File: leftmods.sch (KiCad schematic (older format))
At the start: 13 parts

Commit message: Fix left shift, associate MX footprints
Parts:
- K_LA1, K_LA2, K_LA3, K_LC2, K_LW1, K_LW2: footprint (none) -> MX_Alps_Hybrid:MX-1.5U
- K_LC1: footprint (none) -> MX_Alps_Hybrid:MX-1.25U
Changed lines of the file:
@@
 F 0 "K_LC1" H 4250 4825 60  0000 C CNN
 F 1 "MX-1.25U" H 4250 4750 20  0000 C CNN
-F 2 "" H 4225 4675 60  0001 C CNN
+F 2 "MX_Alps_Hybrid:MX-1.25U" H 4225 4675 60  0001 C CNN
 F 3 "" H 4225 4675 60  0001 C CNN
 	1    4250 4700
@@
 F 0 "K_LC2" H 4250 5400 60  0000 C CNN
 F 1 "MX-1.5U" H 4250 5325 20  0000 C CNN
-F 2 "" H 4225 5250 60  0001 C CNN
+F 2 "MX_Alps_Hybrid:MX-1.5U" H 4225 5250 60  0001 C CNN
 F 3 "" H 4225 5250 60  0001 C CNN
 	1    4250 5275
@@
 F 0 "K_LW2" H 4800 4825 60  0000 C CNN
 F 1 "MX-1.5U" H 4800 4750 20  0000 C CNN
-F 2 "" H 4775 4675 60  0001 C CNN
+F 2 "MX_Alps_Hybrid:MX-1.5U" H 4775 4675 60  0001 C CNN
 F 3 "" H 4775 4675 60  0001 C CNN
 	1    4800 4700
@@
 F 0 "K_LA1" H 4800 5400 60  0000 C CNN
 F 1 "MX-1.5U" H 4800 5325 20  0000 C CNN
-F 2 "" H 4775 5250 60  0001 C CNN
+F 2 "MX_Alps_Hybrid:MX-1.5U" H 4775 5250 60  0001 C CNN
 F 3 "" H 4775 5250 60  0001 C CNN
 	1    4800 5275
@@
 F 0 "K_LW1" H 4800 4250 60  0000 C CNN
 F 1 "MX-1.5U" H 4800 4175 20  0000 C CNN
-F 2 "" H 4775 4100 60  0001 C CNN
+F 2 "MX_Alps_Hybrid:MX-1.5U" H 4775 4100 60  0001 C CNN
 F 3 "" H 4775 4100 60  0001 C CNN
 	1    4800 4125
@@
 F 0 "K_LA2" H 5350 4825 60  0000 C CNN
 F 1 "MX-1.5U" H 5350 4750 20  0000 C CNN
-F 2 "" H 5325 4675 60  0001 C CNN
+F 2 "MX_Alps_Hybrid:MX-1.5U" H 5325 4675 60  0001 C CNN
 F 3 "" H 5325 4675 60  0001 C CNN
 	1    5350 4700
@@
 F 0 "K_LA3" H 5350 5400 60  0000 C CNN
 F 1 "MX-1.5U" H 5350 5325 20  0000 C CNN
-F 2 "" H 5325 5250 60  0001 C CNN
+F 2 "MX_Alps_Hybrid:MX-1.5U" H 5325 5250 60  0001 C CNN
 F 3 "" H 5325 5250 60  0001 C CNN
 	1    5350 5275
@@
 F 0 "DLM1" H 4500 3825 50  0000 C CNN
 F 1 "1N4148WS" H 4500 3625 50  0000 C CNN
-F 2 "" H 4500 3725 50  0000 C CNN
+F 2 "" H 4500 3725 50  0001 C CNN
 F 3 "" H 4500 3725 50  0000 C CNN
 	1    4500 3725
@@
 F 0 "DLM2" H 5050 3825 50  0000 C CNN
 F 1 "1N4148WS" H 5050 3625 50  0000 C CNN
-F 2 "" H 5050 3725 50  0000 C CNN
+F 2 "" H 5050 3725 50  0001 C CNN
 F 3 "" H 5050 3725 50  0000 C CNN
 	1    5050 3725
@@
 F 0 "DLM3" H 5600 3825 50  0000 C CNN
 F 1 "1N4148WS" H 5600 3625 50  0000 C CNN
-F 2 "" H 5600 3725 50  0000 C CNN
+F 2 "" H 5600 3725 50  0001 C CNN
 F 3 "" H 5600 3725 50  0000 C CNN
 	1    5600 3725
@@
 F 0 "RLM1" V 4630 5825 50  0000 C CNN
 F 1 "2.2k" V 4550 5825 50  0000 C CNN
-F 2 "" V 4480 5825 50  0000 C CNN
+F 2 "" V 4480 5825 50  0001 C CNN
 F 3 "" H 4550 5825 50  0000 C CNN
 	1    4550 5825
@@
 F 0 "RLM2" V 5180 5825 50  0000 C CNN
 F 1 "2.2k" V 5100 5825 50  0000 C CNN
-F 2 "" V 5030 5825 50  0000 C CNN
+F 2 "" V 5030 5825 50  0001 C CNN
 F 3 "" H 5100 5825 50  0000 C CNN
 	1    5100 5825
@@
 F 0 "RLM3" V 5730 5825 50  0000 C CNN
 F 1 "2.2k" V 5650 5825 50  0000 C CNN
-F 2 "" V 5580 5825 50  0000 C CNN
+F 2 "" V 5580 5825 50  0001 C CNN
 F 3 "" H 5650 5825 50  0000 C CNN
 	1    5650 5825

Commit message: Laid out PCB
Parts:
- removed K_LA2, K_LW1, K_LW2: MX-1.5U, MX_Alps_Hybrid:MX-1.5U, symbol MX-1.5U
- added K_LA2, K_LW1: MX-1.25U, MX_Alps_Hybrid:MX-1.25U, symbol MX-1.25U
- added K_LW2: MX-1U, MX_Alps_Hybrid:MX-1U, symbol MX-1U
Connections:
- net leftmodsLEDGND: now also K_LA2.4 (LEDGND), K_LW1.4 (LEDGND), K_LW2.4 (LEDGND)
- net leftmodsrow1: now also K_LW1.2 (ROW), K_LW2.2 (ROW)
- net leftmodsrow2: now also K_LA2.2 (ROW)
- net at DLM2.1 (K), K_LA1.1 (COL): now also K_LW1.1 (COL), K_LW2.1 (COL)
- net at K_LA1.3 (LED), RLM2.1: now also K_LW1.3 (LED), K_LW2.3 (LED)
- net at DLM3.1 (K), K_LA3.1 (COL): now also K_LA2.1 (COL)
- net at K_LA3.3 (LED), RLM3.1: now also K_LA2.3 (LED)
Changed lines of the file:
@@
-$EndComp
-$Comp
-L MX-1.5U K_LW2
-U 1 1 591D08D6
-P 4800 4700
-F 0 "K_LW2" H 4800 4825 60  0000 C CNN
-F 1 "MX-1.5U" H 4800 4750 20  0000 C CNN
-F 2 "MX_Alps_Hybrid:MX-1.5U" H 4775 4675 60  0001 C CNN
-F 3 "" H 4775 4675 60  0001 C CNN
-	1    4800 4700
-	1    0    0    -1
 $EndComp
 $Comp
@@
 F 3 "" H 4775 5250 60  0001 C CNN
 	1    4800 5275
-	1    0    0    -1
-$EndComp
-$Comp
-L MX-1.5U K_LW1
-U 1 1 591D095C
-P 4800 4125
-F 0 "K_LW1" H 4800 4250 60  0000 C CNN
-F 1 "MX-1.5U" H 4800 4175 20  0000 C CNN
-F 2 "MX_Alps_Hybrid:MX-1.5U" H 4775 4100 60  0001 C CNN
-F 3 "" H 4775 4100 60  0001 C CNN
-	1    4800 4125
-	1    0    0    -1
-$EndComp
-$Comp
-L MX-1.5U K_LA2
-U 1 1 591D0EC8
-P 5350 4700
-F 0 "K_LA2" H 5350 4825 60  0000 C CNN
-F 1 "MX-1.5U" H 5350 4750 20  0000 C CNN
-F 2 "MX_Alps_Hybrid:MX-1.5U" H 5325 4675 60  0001 C CNN
-F 3 "" H 5325 4675 60  0001 C CNN
-	1    5350 4700
 	1    0    0    -1
 $EndComp
@@
 Wire Wire Line
 	5050 3575 5600 3575
+$Comp
+L MX-1.25U K_LW1
+U 1 1 59494225
+P 4800 4125
+F 0 "K_LW1" H 4800 4250 60  0000 C CNN
+F 1 "MX-1.25U" H 4800 4175 20  0000 C CNN
+F 2 "MX_Alps_Hybrid:MX-1.25U" H 4775 4100 60  0001 C CNN
+F 3 "" H 4775 4100 60  0001 C CNN
+	1    4800 4125
+	1    0    0    -1
+$EndComp
+$Comp
+L MX-1U K_LW2
+U 1 1 59494ACD
+P 4800 4700
+F 0 "K_LW2" H 4800 4825 60  0000 C CNN
+F 1 "MX-1U" H 4800 4750 20  0000 C CNN
+F 2 "MX_Alps_Hybrid:MX-1U" H 4775 4675 60  0001 C CNN
+F 3 "" H 4775 4675 60  0001 C CNN
+	1    4800 4700
+	1    0    0    -1
+$EndComp
+$Comp
+L MX-1.25U K_LA2
+U 1 1 59494B94
+P 5350 4700
+F 0 "K_LA2" H 5350 4825 60  0000 C CNN
+F 1 "MX-1.25U" H 5350 4750 20  0000 C CNN
+F 2 "MX_Alps_Hybrid:MX-1.25U" H 5325 4675 60  0001 C CNN
+F 3 "" H 5325 4675 60  0001 C CNN
+	1    5350 4700
+	1    0    0    -1
+$EndComp
 $EndSCHEMATC

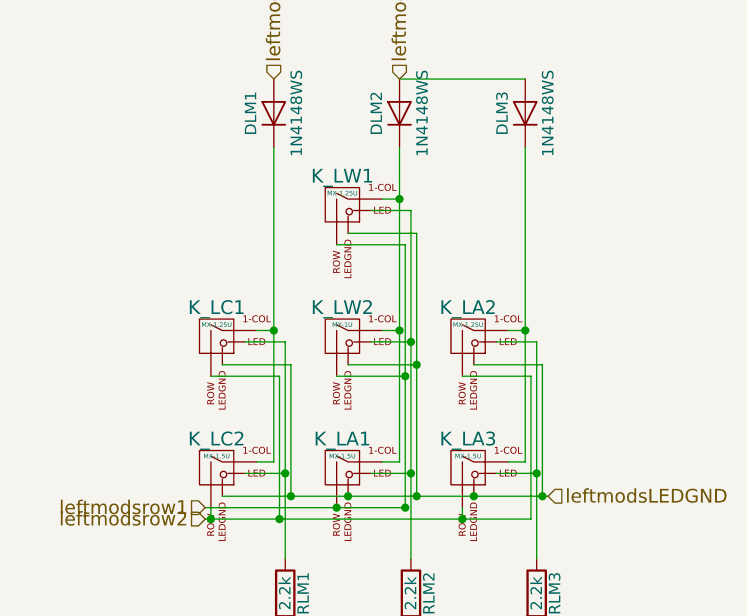
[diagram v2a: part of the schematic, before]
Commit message: Renamed left mods
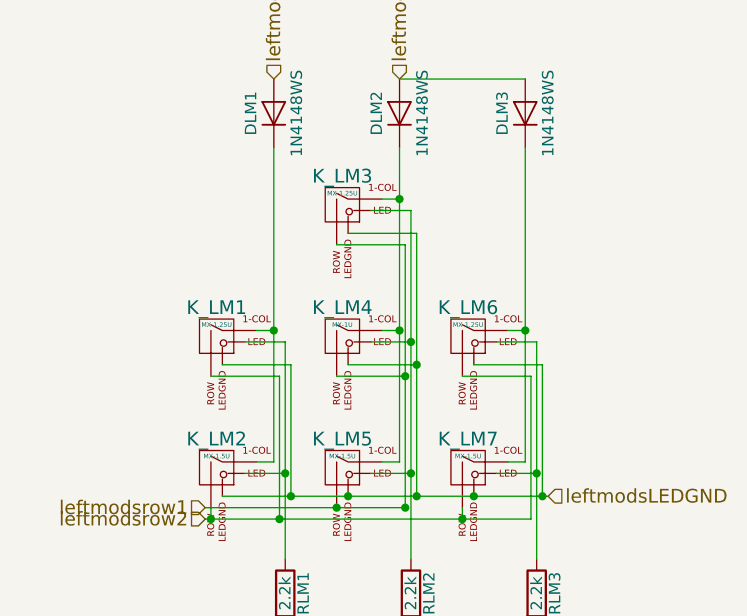
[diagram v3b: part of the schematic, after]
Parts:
- renumbered K_LC1 to K_LM1, K_LC2 to K_LM2, K_LW1 to K_LM3, K_LW2 to K_LM4, K_LA1 to K_LM5, K_LA2 to K_LM6, K_LA3 to K_LM7
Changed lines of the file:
@@
 $EndDescr
 $Comp
-L MX-1.25U K_LC1
+L MX-1.25U K_LM1
 U 1 1 591D07B9
 P 4250 4700
-F 0 "K_LC1" H 4250 4825 60  0000 C CNN
+F 0 "K_LM1" H 4250 4825 60  0000 C CNN
 F 1 "MX-1.25U" H 4250 4750 20  0000 C CNN
 F 2 "MX_Alps_Hybrid:MX-1.25U" H 4225 4675 60  0001 C CNN
@@
 $EndComp
 $Comp
-L MX-1.5U K_LC2
+L MX-1.5U K_LM2
 U 1 1 591D088F
 P 4250 5275
-F 0 "K_LC2" H 4250 5400 60  0000 C CNN
+F 0 "K_LM2" H 4250 5400 60  0000 C CNN
 F 1 "MX-1.5U" H 4250 5325 20  0000 C CNN
 F 2 "MX_Alps_Hybrid:MX-1.5U" H 4225 5250 60  0001 C CNN
@@
 $EndComp
 $Comp
-L MX-1.5U K_LA1
+L MX-1.5U K_LM5
 U 1 1 591D0916
 P 4800 5275
-F 0 "K_LA1" H 4800 5400 60  0000 C CNN
+F 0 "K_LM5" H 4800 5400 60  0000 C CNN
 F 1 "MX-1.5U" H 4800 5325 20  0000 C CNN
 F 2 "MX_Alps_Hybrid:MX-1.5U" H 4775 5250 60  0001 C CNN
@@
 $EndComp
 $Comp
-L MX-1.5U K_LA3
+L MX-1.5U K_LM7
 U 1 1 591D0F45
 P 5350 5275
-F 0 "K_LA3" H 5350 5400 60  0000 C CNN
+F 0 "K_LM7" H 5350 5400 60  0000 C CNN
 F 1 "MX-1.5U" H 5350 5325 20  0000 C CNN
 F 2 "MX_Alps_Hybrid:MX-1.5U" H 5325 5250 60  0001 C CNN
@@
 	5050 3575 5600 3575
 $Comp
-L MX-1.25U K_LW1
+L MX-1.25U K_LM3
 U 1 1 59494225
 P 4800 4125
-F 0 "K_LW1" H 4800 4250 60  0000 C CNN
+F 0 "K_LM3" H 4800 4250 60  0000 C CNN
 F 1 "MX-1.25U" H 4800 4175 20  0000 C CNN
 F 2 "MX_Alps_Hybrid:MX-1.25U" H 4775 4100 60  0001 C CNN
@@
 $EndComp
 $Comp
-L MX-1U K_LW2
+L MX-1U K_LM4
 U 1 1 59494ACD
 P 4800 4700
-F 0 "K_LW2" H 4800 4825 60  0000 C CNN
+F 0 "K_LM4" H 4800 4825 60  0000 C CNN
 F 1 "MX-1U" H 4800 4750 20  0000 C CNN
 F 2 "MX_Alps_Hybrid:MX-1U" H 4775 4675 60  0001 C CNN
@@
 $EndComp
 $Comp
-L MX-1.25U K_LA2
+L MX-1.25U K_LM6
 U 1 1 59494B94
 P 5350 4700
-F 0 "K_LA2" H 5350 4825 60  0000 C CNN
+F 0 "K_LM6" H 5350 4825 60  0000 C CNN
 F 1 "MX-1.25U" H 5350 4750 20  0000 C CNN
 F 2 "MX_Alps_Hybrid:MX-1.25U" H 5325 4675 60  0001 C CNN
